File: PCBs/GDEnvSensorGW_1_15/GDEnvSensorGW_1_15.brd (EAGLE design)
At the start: 66.6 x 29.5 mm, 42 parts, among them CN1 1X4FPC0.5, Q1 NPN, Q2 NPN, U1 3.3V, U3 RFM69HCW, X1 ZX62D-B-5PA8, X2 SMA

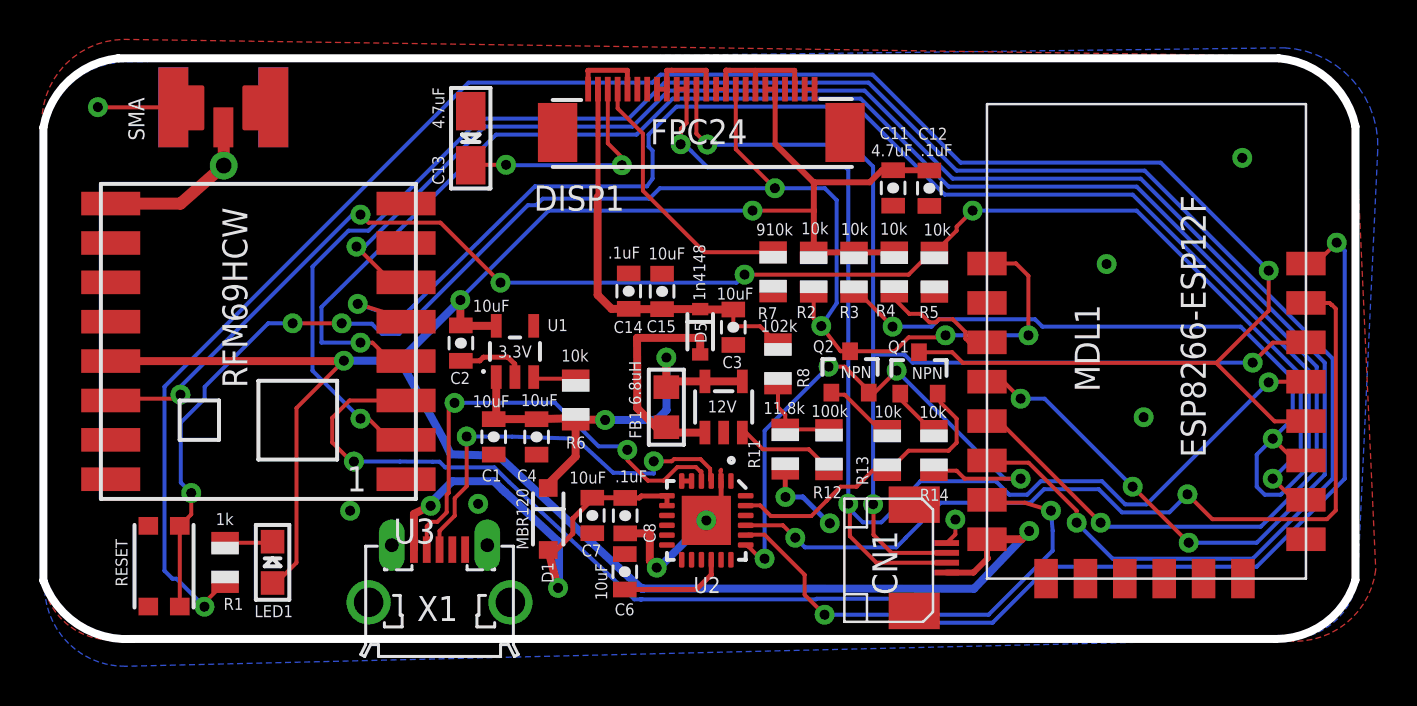
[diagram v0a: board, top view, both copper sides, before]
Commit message: v1.0.5 - bug fix for time display jitter, change topic matching to use strings, reorganize folders
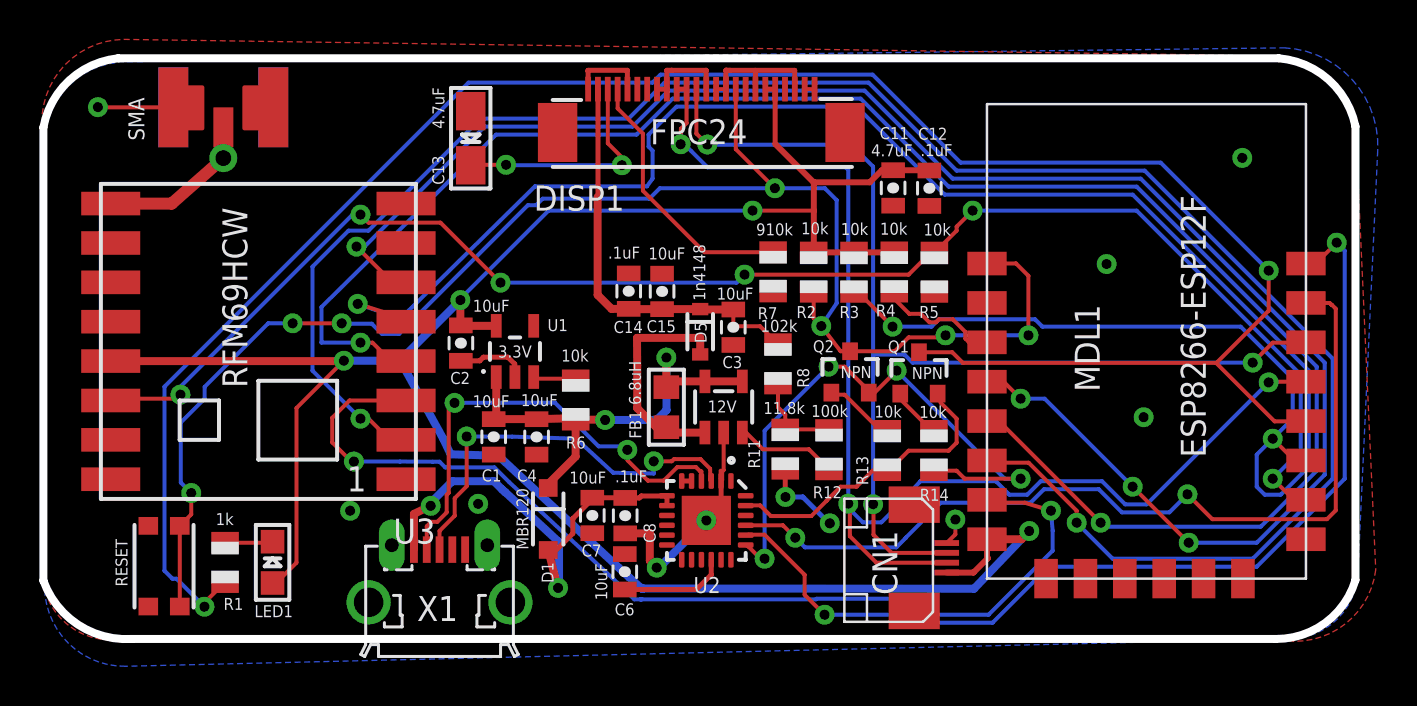
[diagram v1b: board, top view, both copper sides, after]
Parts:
- moved ANT 0.38 mm to (14.4, 24.4)
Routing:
- net GND: track 38.5 -> 40.9 mm
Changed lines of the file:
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@@
 <attribute name="VALUE" x="28.3225" y="14.2815" size="0.6096" layer="21"/>
 </element>
-<element name="ANT" library="LowPowerLab" package="RFM12B-ANTENNA" value="RFM12B_ANTENNA" x="14.389" y="24.03">
-<attribute name="LABEL" value="ANT" x="14.389" y="24.03" size="1.778" layer="27" display="off"/>
+<element name="ANT" library="LowPowerLab" package="RFM12B-ANTENNA" value="RFM12B_ANTENNA" x="14.369" y="24.41">
+<attribute name="LABEL" value="ANT" x="14.369" y="24.41" size="1.778" layer="27" display="off"/>
 </element>
 <element name="FRAME1" library="SparkFun-Aesthetics" package="CREATIVE_COMMONS" value="FRAME-LEDGER" x="6.96" y="-12.12"/>
@@
 <wire x1="39.624" y1="8.5344" x2="39.624" y2="8.128" width="0.2032" layer="1"/>
 <wire x1="39.624" y1="8.128" x2="39.65" y2="8.01" width="0.2032" layer="1"/>
-<wire x1="39.624" y1="8.5344" x2="39.6500125" y2="8.58374375" width="0.2032" layer="1"/>
 <wire x1="34.78" y1="5.35" x2="36.01" y2="5.35" width="0.4064" layer="1"/>
 <wire x1="36.01" y1="5.35" x2="36.03" y2="5.37" width="0.4064" layer="1"/>
@@
 <wire x1="51.5492125" y1="5.2992125" x2="51.5492125" y2="6.053" width="0.2032" layer="1"/>
 <via x="51.5492125" y="6.053" extent="1-16" drill="0.508"/>
+<wire x1="39.78" y1="10.4699" x2="39.78" y2="8.57005" width="0.2032" layer="1"/>
+<wire x1="39.78" y1="8.57005" x2="39.7052" y2="8.49525" width="0.2032" layer="1"/>
+<wire x1="39.7052" y1="8.49525" x2="39.7052" y2="8.0652" width="0.2032" layer="1"/>
+<wire x1="39.7052" y1="8.0652" x2="39.65" y2="8.01" width="0.2032" layer="1"/>
 </signal>
 <signal name="RESET">
@@
 <wire x1="44.5008" y1="2.032" x2="48.5648" y2="2.032" width="0.2032" layer="16"/>
 <wire x1="53.2384" y1="6.9088" x2="53.155" y2="7.053" width="0.2032" layer="1"/>
-<wire x1="23.7744" y1="11.9888" x2="23.65" y2="12.1" width="0.2032" layer="1"/>
 <via x="56.4032" y="6.5028" extent="1-16" drill="0.508"/>
 <wire x1="23.65" y1="12.1" x2="20.78" y2="12.1" width="0.2032" layer="1"/>
@@
 <wire x1="67.46" y1="13.02" x2="61.2628" y2="6.8228" width="0.2032" layer="16"/>
 <via x="67.46" y="13.02" extent="1-16" drill="0.508" diameter="1.016"/>
-<wire x1="69.355" y1="13.053" x2="67.493" y2="13.053" width="0.2032" layer="1"/>
+<wire x1="67.493" y1="13.053" x2="69.355" y2="13.053" width="0.2032" layer="1"/>
 <via x="46.11" y="6.86" extent="1-16" drill="0.508" diameter="1.016"/>
 <wire x1="46.11" y1="6.86" x2="46.11" y2="23.81" width="0.2032" layer="16"/>
@@
 <wire x1="46.19" y1="5.21" x2="46.19" y2="6.78" width="0.2032" layer="1"/>
 <wire x1="46.19" y1="6.78" x2="46.11" y2="6.86" width="0.2032" layer="1"/>
-<wire x1="67.46" y1="13.02" x2="67.493" y2="13.053" width="0" layer="19" extent="1-1"/>
+<wire x1="67.46" y1="13.02" x2="67.493" y2="13.053" width="0.2032" layer="1"/>
 </signal>
 <signal name="ANT">
@@
 <contactref element="U3" pad="9"/>
 <contactref element="X2" pad="P"/>
-<wire x1="8.65" y1="22.1" x2="12.199" y2="22.1" width="0.6096" layer="1"/>
-<wire x1="14.389" y1="24.03" x2="12.199" y2="22.1" width="0.6096" layer="1"/>
-<wire x1="14.37" y1="25.972" x2="14.4" y2="24.301" width="0.6096" layer="1"/>
-<wire x1="14.4" y1="24.301" x2="14.389" y2="24.03" width="0.6096" layer="1"/>
+<wire x1="8.65" y1="22.1" x2="11.747809375" y2="22.1" width="0.6096" layer="1"/>
+<wire x1="14.369" y1="24.41" x2="11.747809375" y2="22.1" width="0.6096" layer="1"/>
+<wire x1="14.37" y1="25.972" x2="14.3891375" y2="24.90609375" width="0.6096" layer="1"/>
+<wire x1="14.3891375" y1="24.90609375" x2="14.369" y2="24.41" width="0.6096" layer="1"/>
 </signal>
 <signal name="N$11">
@@
 <mfgpreviewcolor name="substratecolor" color="0xFF786E46"/>
 </mfgpreviewcolors>
+<errors>
+</errors>
 </board>
 </drawing>

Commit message: Version 1.15 of GW board
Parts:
- removed C15: 10uF, SparkFun-Capacitors:0805-CAP
- added C5: .1uF, SparkFun-Capacitors:0805-CAP
- added IC2: MCP4017T, SamacSys_Parts:SOT65P210X110-6N
- added MIC6122: MIC6122, SamacSys_Parts:SOT95P280X145-5N
- added R10: 22k, adafruit:R0805
- added R15: 13.3K, adafruit:R0805
- added R16, R17: 10k, adafruit:R0805
- added R9: 100K 1%, adafruit:R0805
- added U4: LTR-329, SamacSys_Parts:LTR329ALS01
- R8: value 102k -> 10K 1%
- moved R8 11.1 mm to (32.7, 19.2), turned to 270 degrees
- moved C4 10.9 mm to (41.1, 9.80)
- moved FB1 6.87 mm to (43.5, 13.6), turned to 90 degrees
- moved R11 4.62 mm to (38.5, 11.1)
- moved R7 4.06 mm to (38.3, 19.3)
- moved C14 2.83 mm to (36.8, 15.5), turned to 270 degrees
- moved D5 2.58 mm to (40.9, 16.8), turned to 0 degrees
- moved R6 2.46 mm to (30.5, 10.4)
- moved R2 2.05 mm to (42.4, 19.2)
- moved 12V 2.00 mm to (40.9, 13.4), turned to 180 degrees
- moved C3 2.00 mm to (38.3, 15.5)
- moved C12 1.82 mm to (50.2, 24.7), turned to 90 degrees
- moved C11 1.81 mm to (48.3, 24.7), turned to 90 degrees
- moved R12 1.52 mm to (43.6, 9.85)
- moved Q2 0.72 mm to (46.9, 13.2)
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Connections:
- removed net N$10: R11.2, R12.1, R8.1
- new net N$12: IC2.6, R10.1
- new net N$2: MIC6122.3, R15.1, R8.2
- new net N$6: C5.2, IC2.5, MIC6122.1, R11.2, R12.1
- new net N$7: MIC6122.4, R10.2, R9.1
- net 12V: now also MIC6122.5, R15.2, R9.2; no longer C15.1, R8.2
- net 3.3V: now also 12V.4, 12V.5, C4.2, FB1.1, IC2.1, R16.2, R17.2, U4.1
- net GND: now also C5.1, IC2.2, MIC6122.2, R8.1, U4.2; no longer C15.2
- net SCL: now also IC2.3, R16.1, U4.4
- net SDA: now also IC2.4, R17.1, U4.3
- net VIN_PROT: no longer 12V.4, 12V.5, C4.2, FB1.1
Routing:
- net SCL: track 57.3 -> 110.3 mm, vias 3 -> 10
- net 3.3V: track 121.2 -> 172.7 mm, vias 4 -> 5
- net SDA: track 64.9 -> 105.3 mm, vias 3 -> 8
- net GND: track 40.9 -> 64.0 mm, vias 11 -> 17
- net N$6: track 0.00 -> 18.6 mm, vias 0 -> 2
- net VIN_PROT: track 23.4 -> 7.41 mm, vias 2 -> 0
- net N$12: track 0.00 -> 11.7 mm
- net N$7: track 0.00 -> 10.9 mm, vias 0 -> 2
- net N$8: track 11.6 -> 3.87 mm
- net 12V: track 21.1 -> 28.3 mm, vias 0 -> 2
- net N$15: track 5.17 -> 11.2 mm, vias 0 -> 2
- net N$10: track 4.72 -> 0.00 mm
- net N$2: track 0.00 -> 4.50 mm
- net N$11: track 13.6 -> 9.23 mm
- net D+: track 20.9 -> 24.6 mm
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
